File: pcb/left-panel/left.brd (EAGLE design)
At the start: 15.9 x 57.1 mm, 7 parts, among them J1 SNG-2MM-HEADER-04-V, SW1 B3F-315X, SW2 B3F-315X, SW3 B3F-315X

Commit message: Display base pcb (rev C), Touch panel (rev B)
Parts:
- SW1, SW2, SW3: value B3F-315X -> B3F-3150
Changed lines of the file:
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@@
 </autorouter>
 <elements>
-<element name="SW1" library="Switch" package="B3F-315X" value="B3F-315X" x="4.8006" y="5.715" rot="R270">
+<element name="SW1" library="Switch" package="B3F-315X" value="B3F-3150" x="4.8006" y="5.715" rot="R270">
 <attribute name="PRICE" value="0.21" x="4.8006" y="5.715" size="1.778" layer="27" rot="R270" display="off"/>
+<attribute name="MFG" value="Omron" x="4.8006" y="5.715" size="1.778" layer="27" rot="R270" display="off"/>
 </element>
-<element name="SW2" library="Switch" package="B3F-315X" value="B3F-315X" x="4.8006" y="20.32" rot="R270">
+<element name="SW2" library="Switch" package="B3F-315X" value="B3F-3150" x="4.8006" y="20.32" rot="R270">
 <attribute name="TEST" value="test" x="4.8006" y="20.32" size="1.778" layer="27" rot="R270" display="off"/>
 <attribute name="PRICE" value="0.21" x="4.8006" y="20.32" size="1.778" layer="27" rot="R270" display="off"/>
+<attribute name="MFG" value="Omron" x="4.8006" y="20.32" size="1.778" layer="27" rot="R270" display="off"/>
 </element>
-<element name="SW3" library="Switch" package="B3F-315X" value="B3F-315X" x="4.8006" y="29.845" rot="R270">
+<element name="SW3" library="Switch" package="B3F-315X" value="B3F-3150" x="4.8006" y="29.845" rot="R270">
 <attribute name="PRICE" value="0.21" x="4.8006" y="29.845" size="1.778" layer="27" rot="R270" display="off"/>
+<attribute name="MFG" value="Omron" x="4.8006" y="29.845" size="1.778" layer="27" rot="R270" display="off"/>
 </element>
 <element name="J1" library="Connectors" package="DF3X-4P-2DSA" value="SNG-2MM-HEADER-04-V" x="8.255" y="41.275" rot="R90">

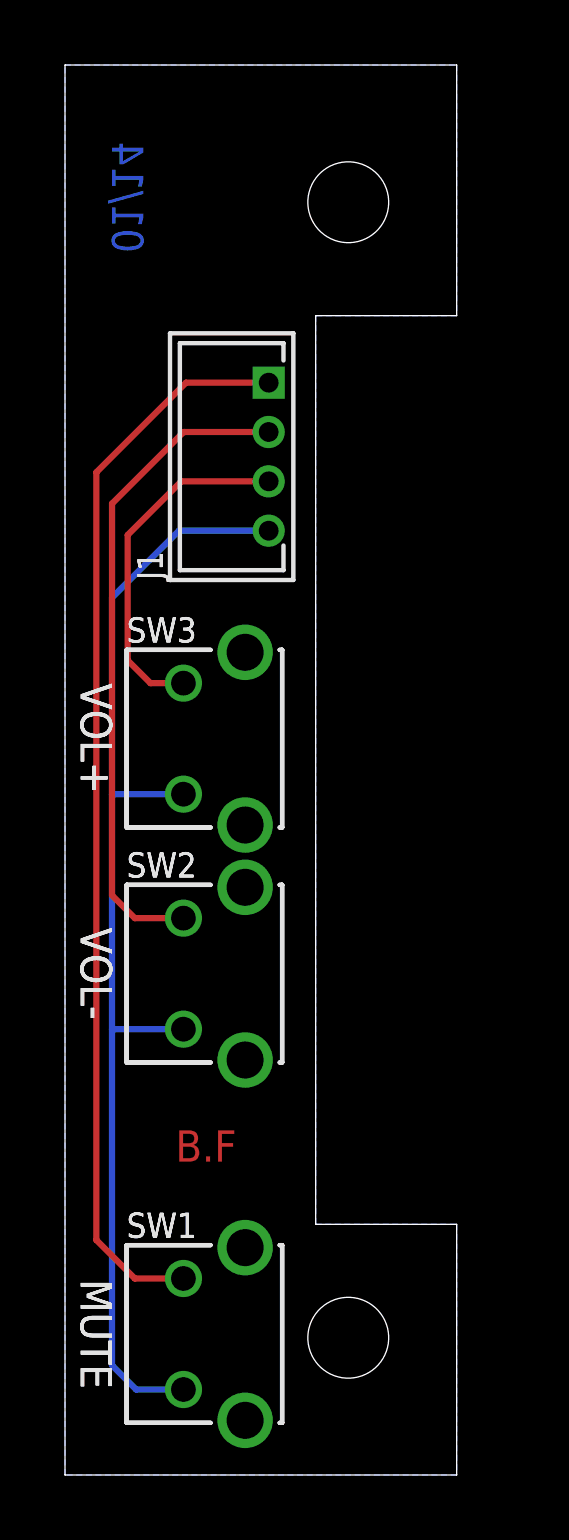
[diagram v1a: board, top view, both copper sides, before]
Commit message: Fixed dimensions error in CLK-DWG-05 (Left panel PCB)
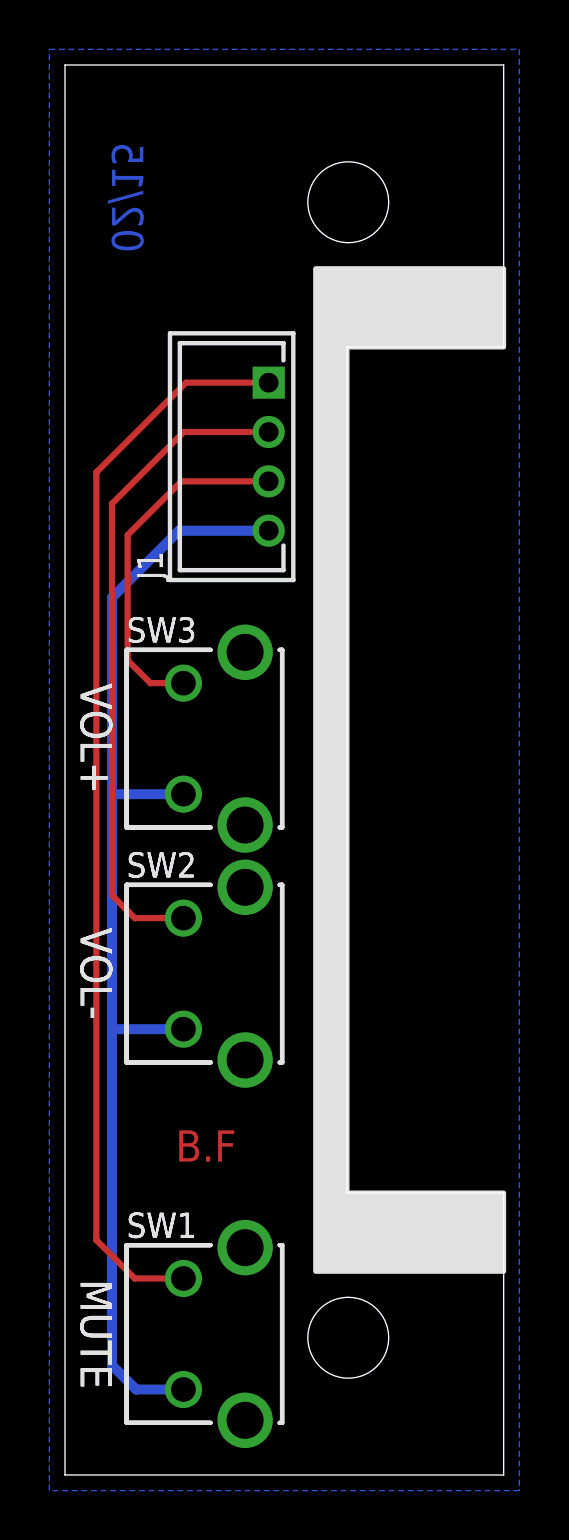
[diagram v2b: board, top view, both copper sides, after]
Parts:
- moved U$3 2.01 mm to (5.08, 50.2)
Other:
- board size 15.9 x 57.1 mm -> 17.8 x 57.1 mm
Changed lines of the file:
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@@
 <layer number="20" name="Dimension" color="15" fill="1" visible="yes" active="yes"/>
 <layer number="21" name="tPlace" color="7" fill="1" visible="yes" active="yes"/>
-<layer number="22" name="bPlace" color="7" fill="1" visible="no" active="yes"/>
+<layer number="22" name="bPlace" color="7" fill="1" visible="yes" active="yes"/>
 <layer number="23" name="tOrigins" color="15" fill="1" visible="yes" active="yes"/>
 <layer number="24" name="bOrigins" color="15" fill="1" visible="yes" active="yes"/>
-<layer number="25" name="tNames" color="7" fill="1" visible="no" active="yes"/>
-<layer number="26" name="bNames" color="7" fill="1" visible="no" active="yes"/>
+<layer number="25" name="tNames" color="7" fill="1" visible="yes" active="yes"/>
+<layer number="26" name="bNames" color="7" fill="1" visible="yes" active="yes"/>
 <layer number="27" name="tValues" color="7" fill="1" visible="no" active="yes"/>
 <layer number="28" name="bValues" color="7" fill="1" visible="no" active="yes"/>
@@
 <layer number="44" name="Drills" color="7" fill="1" visible="no" active="yes"/>
 <layer number="45" name="Holes" color="7" fill="1" visible="yes" active="yes"/>
-<layer number="46" name="Milling" color="3" fill="1" visible="yes" active="yes"/>
+<layer number="46" name="Milling" color="3" fill="1" visible="no" active="yes"/>
 <layer number="47" name="Measures" color="7" fill="1" visible="no" active="yes"/>
 <layer number="48" name="Document" color="7" fill="1" visible="no" active="yes"/>
@@
 <layer number="107" name="BD-Top" color="5" fill="1" visible="no" active="no"/>
 <layer number="116" name="centerDrill" color="7" fill="1" visible="no" active="yes"/>
-<layer number="121" name="_tsilk" color="14" fill="1" visible="yes" active="yes"/>
-<layer number="122" name="_bsilk" color="5" fill="1" visible="yes" active="yes"/>
+<layer number="121" name="_tsilk" color="14" fill="1" visible="no" active="yes"/>
+<layer number="122" name="_bsilk" color="5" fill="1" visible="no" active="yes"/>
 <layer number="200" name="200bmp" color="1" fill="10" visible="no" active="yes"/>
 <layer number="201" name="201bmp" color="2" fill="10" visible="no" active="yes"/>
@@
 <board>
 <plain>
-<wire x1="0" y1="0" x2="15.875" y2="0" width="0" layer="20"/>
-<wire x1="15.875" y1="57.15" x2="0" y2="57.15" width="0" layer="20"/>
+<wire x1="0" y1="0" x2="17.78" y2="0" width="0" layer="20"/>
+<wire x1="17.78" y1="57.15" x2="0" y2="57.15" width="0" layer="20"/>
 <wire x1="0" y1="57.15" x2="0" y2="0" width="0" layer="20"/>
-<wire x1="15.875" y1="57.15" x2="15.875" y2="46.99" width="0" layer="20"/>
-<wire x1="15.875" y1="46.99" x2="10.16" y2="46.99" width="0" layer="20"/>
-<wire x1="10.16" y1="46.99" x2="10.16" y2="10.16" width="0" layer="20"/>
-<wire x1="10.16" y1="10.16" x2="15.875" y2="10.16" width="0" layer="20"/>
-<wire x1="15.875" y1="10.16" x2="15.875" y2="0" width="0" layer="20"/>
+<wire x1="17.78" y1="57.15" x2="17.78" y2="45.72" width="0" layer="20"/>
+<wire x1="17.78" y1="45.72" x2="11.43" y2="45.72" width="0" layer="20"/>
+<wire x1="11.43" y1="45.72" x2="11.43" y2="11.43" width="0" layer="20"/>
+<wire x1="11.43" y1="11.43" x2="17.78" y2="11.43" width="0" layer="20"/>
+<wire x1="17.78" y1="11.43" x2="17.78" y2="0" width="0" layer="20"/>
 <hole x="11.4808" y="5.5626" drill="3.2766"/>
 <hole x="11.4808" y="51.5874" drill="3.2766"/>
@@
 <text x="1.27" y="20.32" size="1.27" layer="121" font="vector" ratio="16" rot="SR270" align="center">VOL-</text>
 <text x="1.27" y="29.845" size="1.27" layer="121" font="vector" ratio="16" rot="SR270" align="center">VOL+</text>
+<rectangle x1="11.43" y1="45.72" x2="17.78" y2="48.895" layer="39"/>
+<rectangle x1="11.43" y1="8.255" x2="17.78" y2="11.43" layer="39"/>
+<rectangle x1="10.16" y1="8.255" x2="11.43" y2="48.895" layer="39"/>
+<polygon width="0.2032" layer="21">
+<vertex x="17.78" y="8.255"/>
+<vertex x="17.78" y="11.43"/>
+<vertex x="11.43" y="11.43"/>
+<vertex x="11.43" y="45.72"/>
+<vertex x="17.78" y="45.72"/>
+<vertex x="17.78" y="48.895"/>
+<vertex x="10.16" y="48.895"/>
+<vertex x="10.16" y="8.255"/>
+</polygon>
 </plain>
 <attributes>
-<attribute name="DATE" value="01/14"/>
+<attribute name="DATE" value="02/15"/>
 </attributes>
 <variantdefs>
@@
 <element name="U$1" library="Symbols" package="INFO_AUTHOR" value="" x="5.715" y="13.335"/>
 <element name="U$2" library="Symbols" package="INFO_DATE" value="" x="1.905" y="49.53" rot="MR90"/>
-<element name="U$3" library="Symbols" package="OPENHW_LOGO_150" value="" x="5.715" y="52.07" rot="MR90"/>
+<element name="U$3" library="Symbols" package="OPENHW_LOGO_150" value="" x="5.08" y="50.165" rot="MR90"/>
 </elements>
 <signals>
@@
 <contactref element="SW3" pad="4"/>
 <polygon width="0.4064" layer="16" isolate="0.4064">
-<vertex x="15.875" y="0"/>
-<vertex x="0" y="0"/>
-<vertex x="0" y="57.15"/>
-<vertex x="15.875" y="57.15"/>
-<vertex x="15.875" y="46.99"/>
-<vertex x="10.16" y="46.99"/>
-<vertex x="10.16" y="10.16"/>
-<vertex x="15.875" y="10.16"/>
+<vertex x="18.415" y="-0.635"/>
+<vertex x="-0.635" y="-0.635"/>
+<vertex x="-0.635" y="57.785"/>
+<vertex x="18.415" y="57.785"/>
 </polygon>
 </signal>
@@
 <contactref element="SW2" pad="2"/>
 <contactref element="SW1" pad="2"/>
-<wire x1="4.8006" y1="3.465" x2="2.885" y2="3.465" width="0.254" layer="16"/>
-<wire x1="2.885" y1="3.465" x2="1.905" y2="4.445" width="0.254" layer="16"/>
-<wire x1="1.905" y1="4.445" x2="1.905" y2="18.07" width="0.254" layer="16"/>
+<wire x1="4.8006" y1="3.465" x2="2.885" y2="3.465" width="0.4064" layer="16"/>
+<wire x1="2.885" y1="3.465" x2="1.905" y2="4.445" width="0.4064" layer="16"/>
+<wire x1="1.905" y1="4.445" x2="1.905" y2="18.07" width="0.4064" layer="16"/>
 <contactref element="J1" pad="4"/>
-<wire x1="1.905" y1="18.07" x2="1.905" y2="27.595" width="0.254" layer="16"/>
-<wire x1="1.905" y1="27.595" x2="1.905" y2="35.56" width="0.254" layer="16"/>
-<wire x1="8.255" y1="38.275" x2="4.62" y2="38.275" width="0.254" layer="16"/>
-<wire x1="4.62" y1="38.275" x2="1.905" y2="35.56" width="0.254" layer="16"/>
-<wire x1="4.8006" y1="27.595" x2="1.905" y2="27.595" width="0.254" layer="16"/>
-<wire x1="4.8006" y1="18.07" x2="1.905" y2="18.07" width="0.254" layer="16"/>
+<wire x1="1.905" y1="18.07" x2="1.905" y2="27.595" width="0.4064" layer="16"/>
+<wire x1="1.905" y1="27.595" x2="1.905" y2="35.56" width="0.4064" layer="16"/>
+<wire x1="8.255" y1="38.275" x2="4.62" y2="38.275" width="0.4064" layer="16"/>
+<wire x1="4.62" y1="38.275" x2="1.905" y2="35.56" width="0.4064" layer="16"/>
+<wire x1="4.8006" y1="27.595" x2="1.905" y2="27.595" width="0.4064" layer="16"/>
+<wire x1="4.8006" y1="18.07" x2="1.905" y2="18.07" width="0.4064" layer="16"/>
 </signal>
 <signal name="MUTE">
